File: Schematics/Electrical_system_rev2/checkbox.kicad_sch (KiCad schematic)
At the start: 29 parts, among them K6 Relay_SPST-NO, U10 TSAL, U8 BSPD, U9 Relay board

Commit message: fixed checkbox
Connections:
- net t1_motor: now also A1.26 (A7)
- net t2_motor: now also A1.25 (A6)
- net t_accum: now also A1.24 (SCL/A5)
- net SDC1 renamed TSMS_check
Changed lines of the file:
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@@
 	)
 	(junction
-		(at 158.75 207.01)
-		(diameter 0)
-		(color 0 0 0 0)
-	)
-	(junction
 		(at 57.15 153.67)
 		(diameter 0)
@@
 	(wire
 		(pts
-			(xy 158.75 207.01) (xy 163.83 207.01)
-		)
-		(stroke
-			(width 0)
-			(type default)
-		)
-	)
-	(wire
-		(pts
 			(xy 68.58 158.75) (xy 85.09 158.75)
 		)
@@
 	(wire
 		(pts
-			(xy 275.59 55.88) (xy 275.59 116.84)
-		)
-		(stroke
-			(width 0)
-			(type default)
-		)
-	)
-	(wire
-		(pts
 			(xy 119.126 66.04) (xy 119.126 62.23)
 		)
@@
 		)
 	)
-	(label "SDC1"
-		(at 275.59 115.57 90)
-		(fields_autoplaced yes)
-		(effects
-			(font
-				(size 1.27 1.27)
-			)
-			(justify left bottom)
-		)
-	)
 	(label "IMD_fault"
 		(at 252.73 120.65 90)
@@
 		)
 	)
-	(global_label "SDC1"
-		(shape output)
-		(at 163.83 207.01 0)
-		(fields_autoplaced yes)
-		(effects
-			(font
-				(size 1.27 1.27)
-			)
-			(justify left)
-		)
-		(property "Intersheetrefs" "${INTERSHEET_REFS}"
-			(at 171.6948 207.01 0)
-			(effects
-				(font
-					(size 1.27 1.27)
-				)
-				(justify left)
-				(hide yes)
-			)
-		)
-	)
 	(global_label "5V_dash"
 		(shape output)
@@
 		)
 	)
+	(global_label "t2_motor"
+		(shape output)
+		(at 234.95 85.09 90)
+		(fields_autoplaced yes)
+		(effects
+			(font
+				(size 1.27 1.27)
+			)
+			(justify left)
+		)
+		(property "Intersheetrefs" "${INTERSHEET_REFS}"
+			(at 234.95 73.6988 90)
+			(effects
+				(font
+					(size 1.27 1.27)
+				)
+				(justify left)
+				(hide yes)
+			)
+		)
+	)
 	(global_label "SDC3"
 		(shape output)
@@
 		)
 	)
+	(global_label "t_accum"
+		(shape output)
+		(at 232.41 85.09 90)
+		(fields_autoplaced yes)
+		(effects
+			(font
+				(size 1.27 1.27)
+			)
+			(justify left)
+		)
+		(property "Intersheetrefs" "${INTERSHEET_REFS}"
+			(at 232.41 74.243 90)
+			(effects
+				(font
+					(size 1.27 1.27)
+				)
+				(justify left)
+				(hide yes)
+			)
+		)
+	)
 	(global_label "GLV+"
 		(shape bidirectional)
@@
 		)
 	)
+	(global_label "t1_motor"
+		(shape output)
+		(at 237.49 85.09 90)
+		(fields_autoplaced yes)
+		(effects
+			(font
+				(size 1.27 1.27)
+			)
+			(justify left)
+		)
+		(property "Intersheetrefs" "${INTERSHEET_REFS}"
+			(at 237.49 73.6988 90)
+			(effects
+				(font
+					(size 1.27 1.27)
+				)
+				(justify left)
+				(hide yes)
+			)
+		)
+	)
 	(global_label "SW"
 		(shape bidirectional)
@@
 		)
 	)
-	(global_label "SDC1"
-		(shape input)
-		(at 275.59 116.84 270)
-		(fields_autoplaced yes)
-		(effects
-			(font
-				(size 1.27 1.27)
-			)
-			(justify right)
-		)
-		(property "Intersheetrefs" "${INTERSHEET_REFS}"
-			(at 275.59 124.7048 90)
-			(effects
-				(font
-					(size 1.27 1.27)
-				)
-				(justify right)
-				(hide yes)
-			)
-		)
-	)
 	(global_label "GLV-"
 		(shape bidirectional)
@@
 		)
 	)
-	(hierarchical_label "SDC1"
-		(shape input)
-		(at 275.59 55.88 90)
-		(fields_autoplaced yes)
-		(effects
-			(font
-				(size 1.27 1.27)
-			)
-			(justify left)
-		)
-	)
 	(hierarchical_label "Brake2"
 		(shape input)
@@
 				)
 			)
-			(project "checkbox"
-				(path "/5ec0699a-3c0f-41bb-8561-c4fd7e59fe9f"
-					(reference "U8")
-					(unit 1)
-				)
-			)
-			(project "checkbox"
-				(path "/66b61c93-6624-4ced-bd06-c7d072a0e2f9"
-					(reference "U1")
-					(unit 1)
-				)
-			)
 			(project "Electrical_system_rev2"
 				(path "/e737253b-bf2e-46db-bb95-366ad16822f4/1c314dd2-2602-4f14-9f58-5b14367adc1b"
@@
 				)
 			)
-			(project "checkbox"
-				(path "/5ec0699a-3c0f-41bb-8561-c4fd7e59fe9f"
-					(reference "U10")
-					(unit 1)
-				)
-			)
-			(project "checkbox"
-				(path "/66b61c93-6624-4ced-bd06-c7d072a0e2f9"
-					(reference "U5")
-					(unit 1)
-				)
-			)
 			(project "Electrical_system_rev2"
 				(path "/e737253b-bf2e-46db-bb95-366ad16822f4/1c314dd2-2602-4f14-9f58-5b14367adc1b"
@@
 	)
 	(symbol
-		(lib_name "FSAE:switch_moduel")
 		(lib_id "FSAE:switch_moduel")
 		(at 139.446 73.66 0)
@@
 	)
 	(symbol
-		(lib_name "FSAE:switch_moduel")
 		(lib_id "FSAE:switch_moduel")
 		(at 119.126 63.5 0)
@@
 				)
 			)
-			(project "checkbox"
-				(path "/5ec0699a-3c0f-41bb-8561-c4fd7e59fe9f"
-					(reference "U11")
-					(unit 1)
-				)
-			)
-			(project "checkbox"
-				(path "/66b61c93-6624-4ced-bd06-c7d072a0e2f9"
-					(reference "U6")
-					(unit 1)
-				)
-			)
 			(project "Electrical_system_rev2"
 				(path "/e737253b-bf2e-46db-bb95-366ad16822f4/1c314dd2-2602-4f14-9f58-5b14367adc1b"
@@
 				)
 			)
-			(project "checkbox"
-				(path "/5ec0699a-3c0f-41bb-8561-c4fd7e59fe9f"
-					(reference "U9")
-					(unit 1)
-				)
-			)
-			(project "checkbox"
-				(path "/66b61c93-6624-4ced-bd06-c7d072a0e2f9"
-					(reference "U2")
-					(unit 1)
-				)
-			)
 			(project "Electrical_system_rev2"
 				(path "/e737253b-bf2e-46db-bb95-366ad16822f4/1c314dd2-2602-4f14-9f58-5b14367adc1b"
@@
 		)
 	)
+	(sheet_instances
+		(path "/"
+			(page "1")
+		)
+	)

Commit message: fixed pwm boards
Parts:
- removed F17: Fuse, symbol Device:Fuse
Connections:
- net GLV+_fan1 is gone; now on net fans_control: U24. (Vout-)
- net GLV+_pump2 is gone; now on net pump2_control: U25. (Vout-)
- new net fan1-: U24. (Vout-)
- new net pump2-: U25. (Vout-)
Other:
- note removed: "7 A"
- note removed: "Fan1"
- note removed: "Fan2"

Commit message: SDC
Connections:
- net SDC2: now also D5.1 (K), K6.A1
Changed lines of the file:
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@@
 	(wire
 		(pts
+			(xy 142.24 199.39) (xy 142.24 214.63)
+		)
+		(stroke
+			(width 0)
+			(type default)
+		)
+	)
+	(wire
+		(pts
 			(xy 262.89 55.88) (xy 262.89 125.73)
 		)
@@
 		)
 	)
+	(global_label "SDC3"
+		(shape input)
+		(at 142.24 199.39 90)
+		(fields_autoplaced yes)
+		(effects
+			(font
+				(size 1.27 1.27)
+			)
+			(justify left)
+		)
+		(property "Intersheetrefs" "${INTERSHEET_REFS}"
+			(at 142.24 191.4458 90)
+			(effects
+				(font
+					(size 1.27 1.27)
+				)
+				(justify left)
+				(hide yes)
+			)
+		)
+	)
 	(global_label "TSMS_check"
 		(shape output)
@@
 		)
 	)
+	(global_label "SDC2"
+		(shape input)
+		(at 81.28 85.09 0)
+		(fields_autoplaced yes)
+		(effects
+			(font
+				(size 1.27 1.27)
+			)
+			(justify left)
+		)
+		(property "Intersheetrefs" "${INTERSHEET_REFS}"
+			(at 89.2242 85.09 0)
+			(effects
+				(font
+					(size 1.27 1.27)
+				)
+				(justify left)
+				(hide yes)
+			)
+		)
+	)
 	(global_label "RD+"
 		(shape bidirectional)
@@
 		)
 	)
+	(hierarchical_label "SDC3"
+		(shape input)
+		(at 142.24 214.63 270)
+		(fields_autoplaced yes)
+		(effects
+			(font
+				(size 1.27 1.27)
+			)
+			(justify right)
+		)
+	)
 	(hierarchical_label "TSMS_in"
 		(shape input)
@@
 		)
 	)
+	(hierarchical_label "GLVMS_in"
+		(shape input)
+		(at 81.28 55.88 90)
+		(fields_autoplaced yes)
+		(effects
+			(font
+				(size 1.27 1.27)
+			)
+			(justify left)
+		)
+	)
 	(hierarchical_label "Throttle2"
 		(shape input)
@@
 	)
 	(symbol
-		(lib_name "FSAE:switch_moduel")
 		(lib_id "FSAE:switch_moduel")
 		(at 139.7 73.66 0)
@@
 	)
 	(symbol
-		(lib_name "FSAE:switch_moduel")
 		(lib_id "FSAE:switch_moduel")
 		(at 119.38 63.5 0)

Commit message: updating of electrical system
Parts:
- removed A1: Arduino_Nano_Every, Module:Arduino_Nano, symbol MCU_Module:Arduino_Nano_Every
- removed R4, R5, R6: 100k, symbol Device:R
- removed U11: ~, symbol FSAE:Emeter
- removed U24, U25: ~, symbol FSAE:switch_moduel
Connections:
- net HV-_to_motor is gone; now on net RD+: U10. (RD+)
- net t1_motor is gone; now on net CANL_250: VCU1.BB2 (CANL0)
- net t_accum is gone; now on net CANH_500: VCU1.BC2 (CANH1)
- net HV-: now also U10. (RD+)
- net GLV+_pump_motor: now reaches F18.2
- net GLV+_fan: now reaches F19.2
- net GLV+_pump1 renamed GLV+_pump_accum
- net fans_control: no longer names the net of VCU1.AF3 (DOUT7)
- net t2_motor: no longer names the net of VCU1.BB1 (AIN5)
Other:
- note added: "12 A-Hr battery"

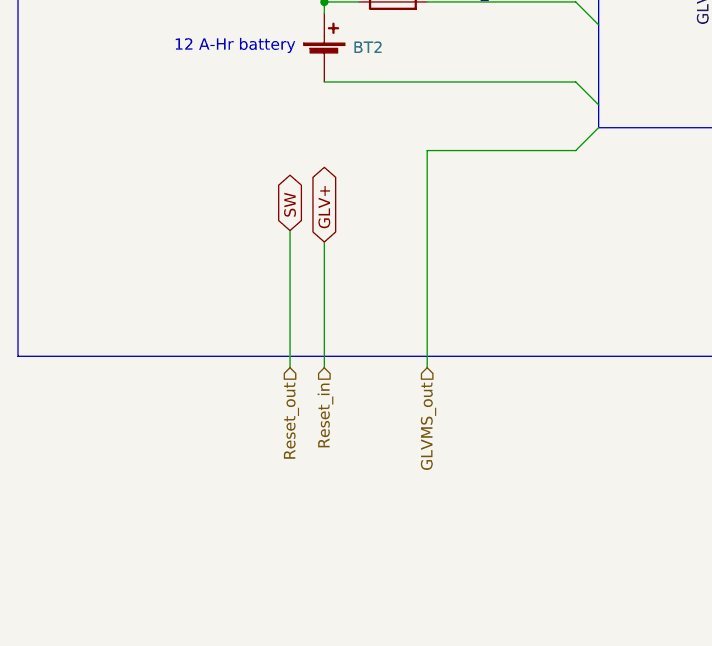
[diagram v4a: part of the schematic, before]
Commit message: fixed reset switch
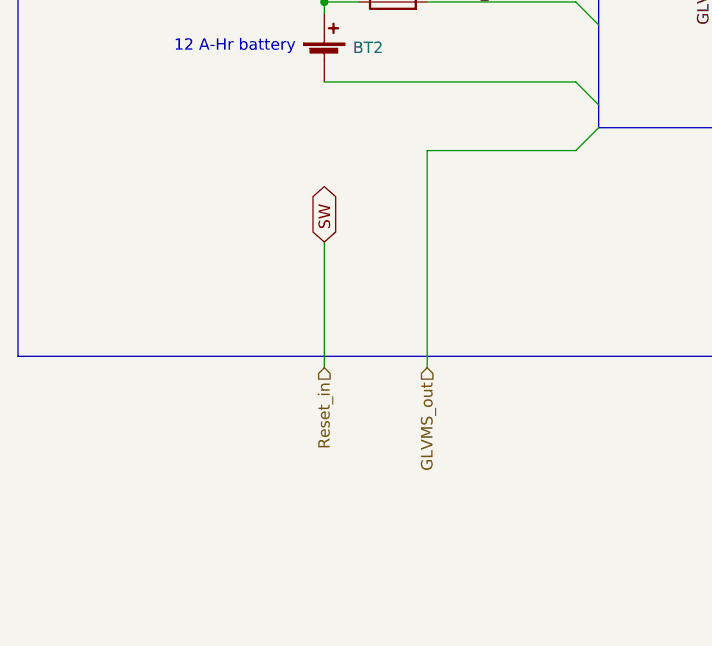
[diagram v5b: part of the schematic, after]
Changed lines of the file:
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@@
-	(wire
-		(pts
-			(xy 53.34 196.85) (xy 53.34 212.09)
-		)
-		(stroke
-			(width 0)
-			(type default)
-		)
-	)
 	(wire
 		(pts
@@
 		)
 	)
-	(global_label "GLV+"
-		(shape bidirectional)
-		(at 57.15 198.12 90)
-		(fields_autoplaced yes)
-		(effects
-			(font
-				(size 1.27 1.27)
-			)
-			(justify left)
-		)
-		(property "Intersheetrefs" "${INTERSHEET_REFS}"
-			(at 57.15 189.0644 90)
-			(effects
-				(font
-					(size 1.27 1.27)
-				)
-				(justify left)
-				(hide yes)
-			)
-		)
-	)
 	(global_label "SDC3"
 		(shape output)
@@
 	(global_label "SW"
 		(shape bidirectional)
-		(at 53.34 196.85 90)
-		(fields_autoplaced yes)
-		(effects
-			(font
-				(size 1.27 1.27)
-			)
-			(justify left)
-		)
-		(property "Intersheetrefs" "${INTERSHEET_REFS}"
-			(at 53.34 190.0926 90)
+		(at 57.15 198.12 90)
+		(fields_autoplaced yes)
+		(effects
+			(font
+				(size 1.27 1.27)
+			)
+			(justify left)
+		)
+		(property "Intersheetrefs" "${INTERSHEET_REFS}"
+			(at 57.15 191.3626 90)
 			(effects
 				(font
@@
 		(fields_autoplaced yes)
 		(effects
-			(font
-				(size 1.27 1.27)
-			)
-			(justify right)
-		)
-	)
-	(hierarchical_label "Reset_out"
-		(shape input)
-		(at 53.34 212.09 270)
-		(fields_autoplaced yes)
-		(effects

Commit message: updated numberings
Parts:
- renumbered BT5 to BT1, BT1 to BT2, BT2 to BT3, D5 to D7, F7 to F10, F9 to F11, F10 to F12, F11 to F13, F8 to F14, F5 to F15, F21 to F4, F20 to F5, F19 to F6, F18 to F7, F4 to F8, F6 to F9, K6 to K5
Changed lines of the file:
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@@
 		(dnp no)
 		(fields_autoplaced yes)
-		(property "Reference" "F6"
+		(property "Reference" "F9"
 			(at 64.77 144.145 90)
 			(effects
@@
 			(project "Electrical_system_rev2"
 				(path "/e737253b-bf2e-46db-bb95-366ad16822f4/1c314dd2-2602-4f14-9f58-5b14367adc1b"
-					(reference "F6")
+					(reference "F9")
 					(unit 1)
 				)
@@
 			(project "Electrical_system_rev2"
 				(path "/e737253b-bf2e-46db-bb95-366ad16822f4/1c314dd2-2602-4f14-9f58-5b14367adc1b"
-					(reference "U15")
+					(reference "U21")
 					(unit 1)
 				)
@@
 		(dnp no)
 		(fields_autoplaced yes)
-		(property "Reference" "F11"
+		(property "Reference" "F13"
 			(at 64.77 158.115 90)
 			(effects
@@
 			(project "Electrical_system_rev2"
 				(path "/e737253b-bf2e-46db-bb95-366ad16822f4/1c314dd2-2602-4f14-9f58-5b14367adc1b"
-					(reference "F11")
+					(reference "F13")
 					(unit 1)
 				)
@@
 			(project "Electrical_system_rev2"
 				(path "/e737253b-bf2e-46db-bb95-366ad16822f4/1c314dd2-2602-4f14-9f58-5b14367adc1b"
-					(reference "U17")
+					(reference "U23")
 					(unit 1)
 				)
@@
 		(dnp no)
 		(fields_autoplaced yes)
-		(property "Reference" "#PWR027"
+		(property "Reference" "#PWR019"
 			(at 48.26 80.01 0)
 			(effects
@@
 			(project "Electrical_system_rev2"
 				(path "/e737253b-bf2e-46db-bb95-366ad16822f4/1c314dd2-2602-4f14-9f58-5b14367adc1b"
-					(reference "#PWR027")
+					(reference "#PWR019")
 					(unit 1)
 				)
@@
 		(dnp no)
 		(fields_autoplaced yes)
-		(property "Reference" "#PWR025"
+		(property "Reference" "#PWR020"
 			(at 66.04 80.01 0)
 			(effects
@@
 			(project "Electrical_system_rev2"
 				(path "/e737253b-bf2e-46db-bb95-366ad16822f4/1c314dd2-2602-4f14-9f58-5b14367adc1b"
-					(reference "#PWR025")
+					(reference "#PWR020")
 					(unit 1)
 				)
@@
 		(on_board yes)
 		(dnp no)
-		(property "Reference" "F18"
+		(property "Reference" "F7"
 			(at 115.57 106.172 0)
 			(effects
@@
 			(project "Electrical_system_rev2"
 				(path "/e737253b-bf2e-46db-bb95-366ad16822f4/1c314dd2-2602-4f14-9f58-5b14367adc1b"
-					(reference "F18")
+					(reference "F7")
 					(unit 1)
 				)
@@
 		(on_board yes)
 		(dnp no)
-		(property "Reference" "F20"
+		(property "Reference" "F5"
 			(at 102.235 106.045 0)
 			(effects
@@
 			(project "Electrical_system_rev2"
 				(path "/e737253b-bf2e-46db-bb95-366ad16822f4/1c314dd2-2602-4f14-9f58-5b14367adc1b"
-					(reference "F20")
+					(reference "F5")
 					(unit 1)
 				)
@@
 		(dnp no)
 		(fields_autoplaced yes)
-		(property "Reference" "#PWR08"
+		(property "Reference" "#PWR022"
 			(at 332.74 176.53 0)
 			(effects
@@
 			(project "Electrical_system_rev2"
 				(path "/e737253b-bf2e-46db-bb95-366ad16822f4/1c314dd2-2602-4f14-9f58-5b14367adc1b"
-					(reference "#PWR08")
+					(reference "#PWR022")
 					(unit 1)
 				)
@@
 		(on_board yes)
 		(dnp no)
-		(property "Reference" "BT2"
+		(property "Reference" "BT3"
 			(at 60.325 176.53 0)
 			(effects
@@
 			(project "Electrical_system_rev2"
 				(path "/e737253b-bf2e-46db-bb95-366ad16822f4/1c314dd2-2602-4f14-9f58-5b14367adc1b"
-					(reference "BT2")
+					(reference "BT3")
 					(unit 1)
 				)
@@
 		(on_board yes)
 		(dnp no)
-		(property "Reference" "F9"
+		(property "Reference" "F11"
 			(at 64.77 149.225 90)
 			(effects
@@
 			(project "Electrical_system_rev2"
 				(path "/e737253b-bf2e-46db-bb95-366ad16822f4/1c314dd2-2602-4f14-9f58-5b14367adc1b"
-					(reference "F9")
+					(reference "F11")
 					(unit 1)
 				)
@@
 		(on_board yes)
 		(dnp no)
-		(property "Reference" "F21"
+		(property "Reference" "F4"
 			(at 95.885 106.045 0)
 			(effects
@@
 			(project "Electrical_system_rev2"
 				(path "/e737253b-bf2e-46db-bb95-366ad16822f4/1c314dd2-2602-4f14-9f58-5b14367adc1b"
-					(reference "F21")
+					(reference "F4")
 					(unit 1)
 				)
@@
 		(dnp no)
 		(fields_autoplaced yes)
-		(property "Reference" "#PWR012"
+		(property "Reference" "#PWR021"
 			(at 102.87 171.45 0)
 			(effects
@@
 			(project "Electrical_system_rev2"
 				(path "/e737253b-bf2e-46db-bb95-366ad16822f4/1c314dd2-2602-4f14-9f58-5b14367adc1b"
-					(reference "#PWR012")
+					(reference "#PWR021")
 					(unit 1)
 				)
@@
 		(on_board yes)
 		(dnp no)
-		(property "Reference" "F19"
+		(property "Reference" "F6"
 			(at 109.855 106.045 0)
 			(effects
@@
 			(project "Electrical_system_rev2"
 				(path "/e737253b-bf2e-46db-bb95-366ad16822f4/1c314dd2-2602-4f14-9f58-5b14367adc1b"
-					(reference "F19")
+					(reference "F6")
 					(unit 1)
 				)
@@
 		(dnp no)
 		(fields_autoplaced yes)
-		(property "Reference" "F7"
+		(property "Reference" "F10"
 			(at 64.77 146.685 90)
 			(effects
@@
 			(project "Electrical_system_rev2"
 				(path "/e737253b-bf2e-46db-bb95-366ad16822f4/1c314dd2-2602-4f14-9f58-5b14367adc1b"
-					(reference "F7")
+					(reference "F10")
 					(unit 1)
 				)
@@
 		(dnp no)
 		(fields_autoplaced yes)
-		(property "Reference" "D5"
+		(property "Reference" "D7"
 			(at 73.66 101.6 0)
 			(effects
@@
 			(project "Electrical_system_rev2"
 				(path "/e737253b-bf2e-46db-bb95-366ad16822f4/1c314dd2-2602-4f14-9f58-5b14367adc1b"
-					(reference "D5")
+					(reference "D7")
 					(unit 1)
 				)
@@
 		(on_board yes)
 		(dnp no)
-		(property "Reference" "BT1"
+		(property "Reference" "BT2"
 			(at 50.8 99.06 0)
 			(effects
@@
 			(project "Electrical_system_rev2"
 				(path "/e737253b-bf2e-46db-bb95-366ad16822f4/1c314dd2-2602-4f14-9f58-5b14367adc1b"
-					(reference "BT1")
+					(reference "BT2")
 					(unit 1)
 				)
@@
 		(dnp no)
 		(fields_autoplaced yes)
-		(property "Reference" "F5"
+		(property "Reference" "F15"
 			(at 64.77 167.005 90)
 			(effects
@@
 			(project "Electrical_system_rev2"
 				(path "/e737253b-bf2e-46db-bb95-366ad16822f4/1c314dd2-2602-4f14-9f58-5b14367adc1b"
-					(reference "F5")
+					(reference "F15")
 					(unit 1)
 				)
@@
 		(dnp no)
 		(fields_autoplaced yes)
-		(property "Reference" "K6"
+		(property "Reference" "K5"
 			(at 73.66 124.46 90)
 			(effects
@@
 			(project "Electrical_system_rev2"
 				(path "/e737253b-bf2e-46db-bb95-366ad16822f4/1c314dd2-2602-4f14-9f58-5b14367adc1b"
-					(reference "K6")
+					(reference "K5")
 					(unit 1)
 				)
@@
 			(project "Electrical_system_rev2"
 				(path "/e737253b-bf2e-46db-bb95-366ad16822f4/1c314dd2-2602-4f14-9f58-5b14367adc1b"
-					(reference "U16")
+					(reference "U22")
 					(unit 1)
 				)
@@
 		(dnp no)
 		(fields_autoplaced yes)
-		(property "Reference" "BT5"
+		(property "Reference" "BT1"
 			(at 39.37 99.187 0)
 			(effects
@@
 			(project "Electrical_system_rev2"
 				(path "/e737253b-bf2e-46db-bb95-366ad16822f4/1c314dd2-2602-4f14-9f58-5b14367adc1b"
-					(reference "BT5")
+					(reference "BT1")
 					(unit 1)
 				)
@@
 		(dnp no)
 		(fields_autoplaced yes)
-		(property "Reference" "F10"
+		(property "Reference" "F12"
 			(at 64.77 154.305 90)
 			(effects
@@
 			(project "Electrical_system_rev2"
 				(path "/e737253b-bf2e-46db-bb95-366ad16822f4/1c314dd2-2602-4f14-9f58-5b14367adc1b"
-					(reference "F10")
+					(reference "F12")
 					(unit 1)
 				)
@@
 		(dnp no)
 		(fields_autoplaced yes)
-		(property "Reference" "F8"
+		(property "Reference" "F14"
 			(at 64.77 161.925 90)
 			(effects
@@
 			(project "Electrical_system_rev2"
 				(path "/e737253b-bf2e-46db-bb95-366ad16822f4/1c314dd2-2602-4f14-9f58-5b14367adc1b"
-					(reference "F8")
+					(reference "F14")
 					(unit 1)
 				)
@@
 		(dnp no)
 		(fields_autoplaced yes)
-		(property "Reference" "F4"
+		(property "Reference" "F8"
 			(at 64.77 137.795 90)
 			(effects
@@
 			(project "Electrical_system_rev2"
 				(path "/e737253b-bf2e-46db-bb95-366ad16822f4/1c314dd2-2602-4f14-9f58-5b14367adc1b"
-					(reference "F4")
-					(unit 1)
-				)
+					(reference "F8")
+					(unit 1)
+				)
